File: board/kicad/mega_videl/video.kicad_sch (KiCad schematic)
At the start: 18 parts, among them U15 PCA9546APWR, U19 TMDS1204IRNQR, U20 TPD4E02B04DQA, U21 TPD4E02B04DQA, U22 TPD4E02B04DQA, U8 XLH335074.250000X

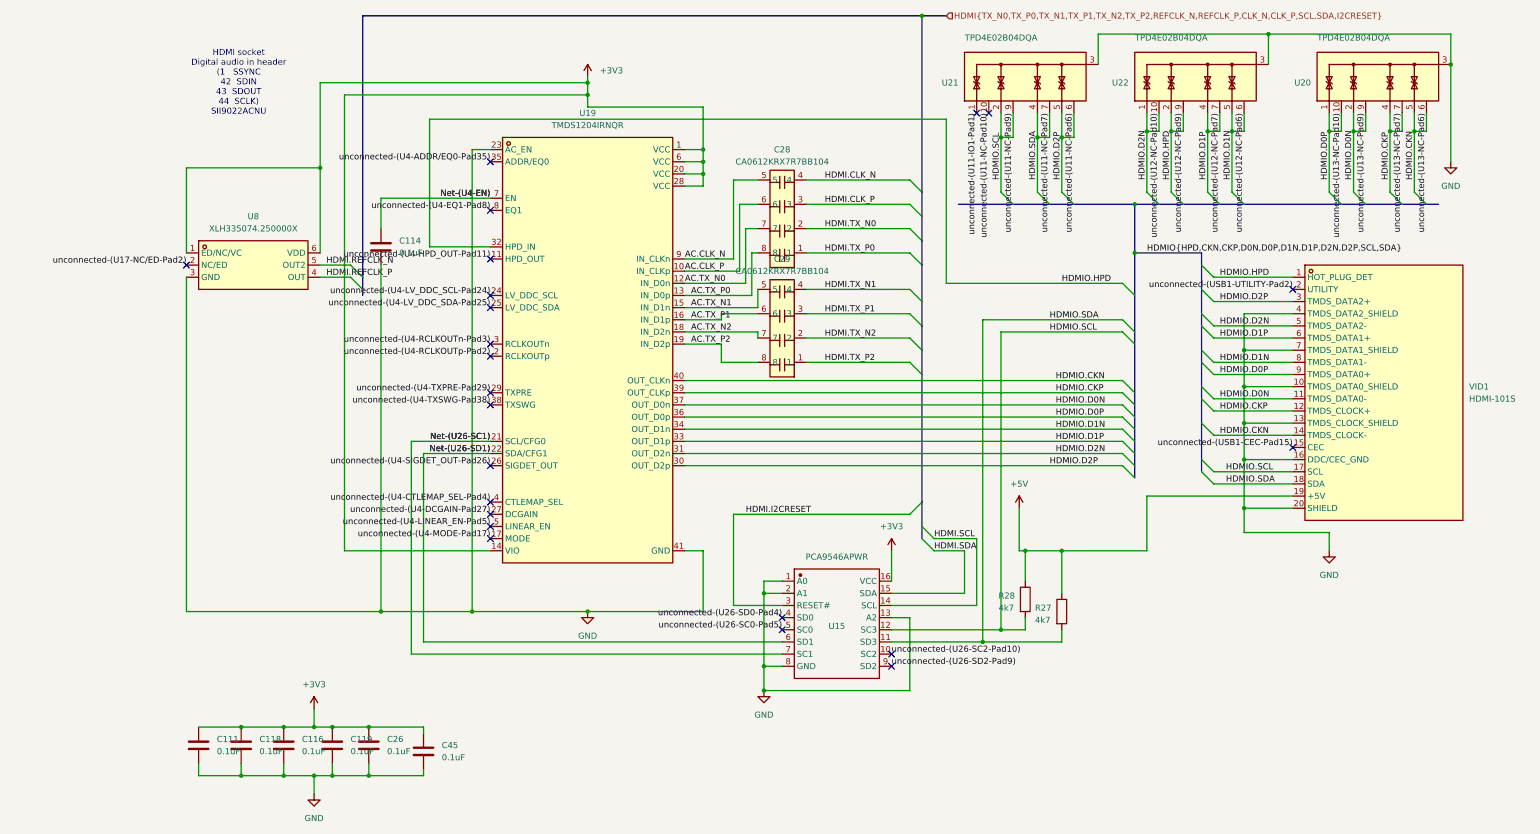
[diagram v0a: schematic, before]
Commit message: Reviewed and fixed many issues. e.g. missing decoupling for 1.35v under fpga
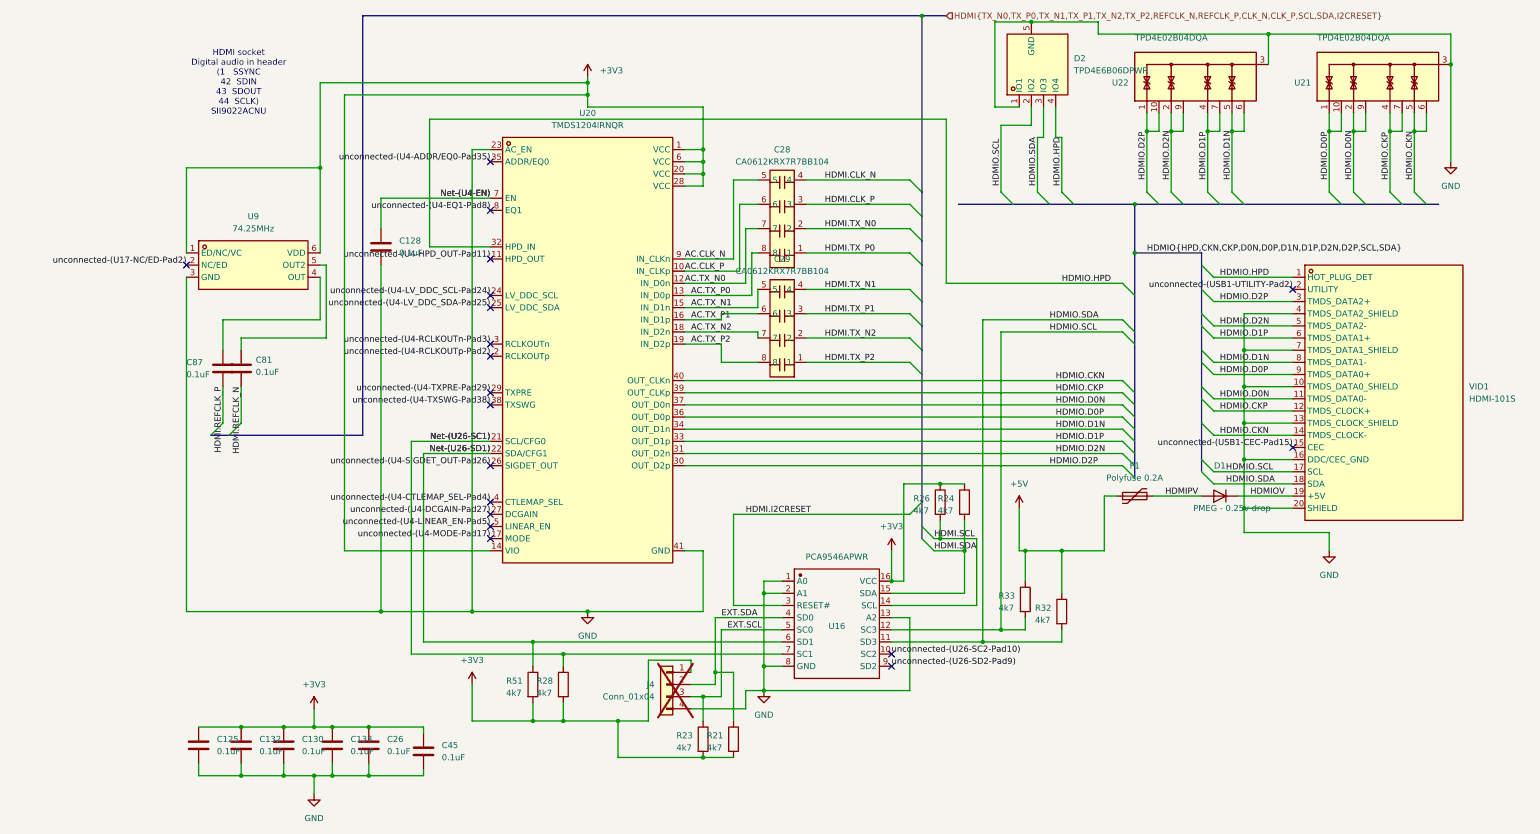
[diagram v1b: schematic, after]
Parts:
- removed U21: TPD4E02B04DQA, Package_SON:USON-10_2.5x1.0mm_P0.5mm, symbol Power_Protection:TPD4E02B04DQA
- added C81, C87: 0.1uF, Capacitor_SMD:C_0402_1005Metric, symbol Device:C
- added D1: PMEG - 0.25v drop, Diode_SMD:D_0603_1608Metric, symbol Device:D
- added D2: TPD4E6B06DPWR, mega_videl:X2SON-4_L0.8-W0.8-P0.48-TL-A, symbol mega_videl:TPD4E6B06DPWR
- added F1: Polyfuse 0.2A, Resistor_SMD:R_0603_1608Metric, symbol Device:Polyfuse
- added J4: Conn_01x04, Connector_PinHeader_2.54mm:PinHeader_1x04_P2.54mm_Vertical, symbol Connector_Generic:Conn_01x04
- added R21, R23, R24, R26, R28, R51: 4k7, Resistor_SMD:R_0603_1608Metric, symbol Device:R
- U16: renamed from U15; LCSC Part (none) -> C400705
- U9: renamed from U8; value XLH335074.250000X -> 74.25MHz; LCSC Part C1883920 -> C836732; MPN XLH335074.250000X -> SiT9121AC-2B2-33E74.250000; Manufacturer RENESAS(瑞萨)/IDT -> SiTime
- renumbered C111 to C125, C114 to C128, C116 to C130, C118 to C132, C119 to C133, R27 to R32, R28 to R33, U19 to U20, U20 to U21
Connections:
- net +3V3: now also J4.1 (Pin_1), R21.2, R23.2, R24.1, R26.1, R28.2, R51.2
- net +5V: now also F1.1; no longer VID1.19 (+5V)
- net GND: now also D2.1 (IO1), D2.5 (GND), J4.4 (Pin_4)
- net HDMI.REFCLK_N: now also C81.1; no longer U9.5 (OUT2)
- net HDMI.REFCLK_P: now also C87.1; no longer U9.4 (OUT)
- net HDMI.SCL: now also R26.2
- net HDMI.SDA: now also R24.2
- net HDMIO.D2N: now also U22.2 (IO2), U22.9 (NC); no longer U22.1 (IO1), U22.10 (NC)
- net HDMIO.D2P: now also U22.1 (IO1), U22.10 (NC)
- net HDMIO.HPD: now also D2.4 (IO4); no longer U22.2 (IO2), U22.9 (NC)
- net HDMIO.SCL: now also D2.2 (IO2)
- net HDMIO.SDA: now also D2.3 (IO3)
- net Net-(U26-SC1): now also R28.1
- net Net-(U26-SD1): now also R51.1
- net unconnected-(U26-SC0-Pad5) renamed EXT.SCL
- net EXT.SCL: now also J4.3 (Pin_3), R23.1
- net unconnected-(U26-SD0-Pad4) renamed EXT.SDA
- net EXT.SDA: now also J4.2 (Pin_2), R21.1
- new net: C81.2, U9.5 (OUT2)
- new net: C87.2, U9.4 (OUT)
- new net HDMIOV: D1.1 (K), VID1.19 (+5V)
- new net HDMIPV: D1.2 (A), F1.2
- no-connect marks 23 -> 19

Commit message: Assigned all parts with JLCPCB plugin
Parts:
- C125, C128, C130, C132, C133, C26, C45: LCSC (none) -> C14663
- C81, C87: LCSC (none) -> C1525
- D1: footprint Diode_SMD:D_0603_1608Metric -> Diode_SMD:D_SOD-323; LCSC (none) -> C7420331
- F1: LCSC (none) -> C207011
- R21, R23, R24, R26, R28, R32, R33, R51: LCSC (none) -> C23162
- U21, U22: LCSC (none) -> C106794
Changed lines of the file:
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@@
 			)
 		)
-		(property "Footprint" "Diode_SMD:D_0603_1608Metric"
+		(property "Footprint" "Diode_SMD:D_SOD-323"
 			(at 232.41 128.27 0)
 			(hide yes)
@@
 			)
 		)
+		(property "LCSC" "C7420331"
+			(at 232.41 128.27 0)
+			(hide yes)
+			(show_name no)
+			(do_not_autoplace no)
+			(effects
+				(font
+					(size 1.27 1.27)
+				)
+			)
+		)
 		(pin "1"
 		)
@@
 			)
 		)
+		(property "LCSC" "C14663"
+			(at 66.04 181.61 0)
+			(hide yes)
+			(show_name no)
+			(do_not_autoplace no)
+			(effects
+				(font
+					(size 1.27 1.27)
+				)
+			)
+		)
 		(pin "1"
 		)
@@
 			)
 		)
+		(property "LCSC" "C23162"
+			(at 179.07 129.54 0)
+			(hide yes)
+			(show_name no)
+			(do_not_autoplace no)
+			(effects
+				(font
+					(size 1.27 1.27)
+				)
+			)
+		)
 		(pin "1"
 		)
@@
 			)
 		)
+		(property "LCSC" "C1525"
+			(at 27.94 101.6 0)
+			(hide yes)
+			(show_name no)
+			(do_not_autoplace no)
+			(effects
+				(font
+					(size 1.27 1.27)
+				)
+			)
+		)
 		(pin "1"
 		)
@@
 			)
 		)
+		(property "LCSC" "C14663"
+			(at 54.61 180.34 0)
+			(hide yes)
+			(show_name no)
+			(do_not_autoplace no)
+			(effects
+				(font
+					(size 1.27 1.27)
+				)
+			)
+		)
 		(pin "1"
 		)
@@
 			)
 		)
+		(property "LCSC" "C23162"
+			(at 199.39 152.4 0)
+			(hide yes)
+			(show_name no)
+			(do_not_autoplace no)
+			(effects
+				(font
+					(size 1.27 1.27)
+				)
+			)
+		)
 		(pin "1"
 		)
@@
 			)
 		)
+		(property "LCSC" "C23162"
+			(at 130.81 179.07 0)
+			(hide yes)
+			(show_name no)
+			(do_not_autoplace no)
+			(effects
+				(font
+					(size 1.27 1.27)
+				)
+			)
+		)
 		(pin "1"
 		)
@@
 			)
 		)
+		(property "LCSC" "C1525"
+			(at 24.13 101.6 0)
+			(hide yes)
+			(show_name no)
+			(do_not_autoplace no)
+			(effects
+				(font
+					(size 1.27 1.27)
+				)
+			)
+		)
 		(pin "1"
 		)
@@
 			)
 		)
+		(property "LCSC" "C23162"
+			(at 88.9 167.64 0)
+			(hide yes)
+			(show_name no)
+			(do_not_autoplace no)
+			(effects
+				(font
+					(size 1.27 1.27)
+				)
+			)
+		)
 		(pin "1"
 		)
@@
 			)
 		)
+		(property "LCSC" "C14663"
+			(at 46.99 180.34 0)
+			(hide yes)
+			(show_name no)
+			(do_not_autoplace no)
+			(effects
+				(font
+					(size 1.27 1.27)
+				)
+			)
+		)
 		(pin "1"
 		)
@@
 			)
 		)
+		(property "LCSC" "C23162"
+			(at 124.46 179.07 0)
+			(hide yes)
+			(show_name no)
+			(do_not_autoplace no)
+			(effects
+				(font
+					(size 1.27 1.27)
+				)
+			)
+		)
 		(pin "1"
 		)
@@
 			)
 		)
+		(property "LCSC" "C23162"
+			(at 173.99 129.54 0)
+			(hide yes)
+			(show_name no)
+			(do_not_autoplace no)
+			(effects
+				(font
+					(size 1.27 1.27)
+				)
+			)
+		)
 		(pin "1"
 		)
@@
 			)
 		)
+		(property "LCSC" "C106794"
+			(at 265.43 40.64 0)
+			(hide yes)
+			(show_name no)
+			(do_not_autoplace no)
+			(effects
+				(font
+					(size 1.27 1.27)
+				)
+			)
+		)
 		(pin "4"
 		)
@@
 			)
 		)
+		(property "LCSC" "C207011"
+			(at 214.63 128.27 0)
+			(hide yes)
+			(show_name no)
+			(do_not_autoplace no)
+			(effects
+				(font
+					(size 1.27 1.27)
+				)
+			)
+		)
 		(pin "1"
 		)
@@
 			)
 		)
+		(property "LCSC" "C14663"
+			(at 36.83 180.34 0)
+			(hide yes)
+			(show_name no)
+			(do_not_autoplace no)
+			(effects
+				(font
+					(size 1.27 1.27)
+				)
+			)
+		)
 		(pin "1"
 		)
@@
 			)
 		)
+		(property "LCSC" "C14663"
+			(at 27.94 180.34 0)
+			(hide yes)
+			(show_name no)
+			(do_not_autoplace no)
+			(effects
+				(font
+					(size 1.27 1.27)
+				)
+			)
+		)
 		(pin "1"
 		)
@@
 			)
 		)
+		(property "LCSC" "C106794"
+			(at 227.33 40.64 0)
+			(hide yes)
+			(show_name no)
+			(do_not_autoplace no)
+			(effects
+				(font
+					(size 1.27 1.27)
+				)
+			)
+		)
 		(pin "4"
 		)
@@
 			)
 		)
+		(property "LCSC" "C23162"
+			(at 191.77 149.86 0)
+			(hide yes)
+			(show_name no)
+			(do_not_autoplace no)
+			(effects
+				(font
+					(size 1.27 1.27)
+				)
+			)
+		)
 		(pin "1"
 		)
@@
 			)
 		)
+		(property "LCSC" "C14663"
+			(at 19.05 180.34 0)
+			(hide yes)
+			(show_name no)
+			(do_not_autoplace no)
+			(effects
+				(font
+					(size 1.27 1.27)
+				)
+			)
+		)
 		(pin "1"
 		)
@@
 			)
 		)
+		(property "LCSC" "C23162"
+			(at 95.25 167.64 0)
+			(hide yes)
+			(show_name no)
+			(do_not_autoplace no)
+			(effects
+				(font
+					(size 1.27 1.27)
+				)
+			)
+		)
 		(pin "1"
 		)
@@
 			(at 57.15 76.2 0)
 			(hide yes)
+			(show_name no)
+			(do_not_autoplace no)
+			(effects
+				(font
+					(size 1.27 1.27)
+				)
+			)
+		)
+		(property "LCSC" "C14663"
+			(at 57.15 76.2 0)
+			(hide yes)

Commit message: Added series resistors to all CT lines. They ring up to 7V apparently according to Super Videl devs. Some of that is likely the length of scope lines. The safety fix here is to add small 33ohm resistors and to enable clamp diodes in the FPGA core.
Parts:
- U20: LCSC Part C20345954 -> C19272424
- renumbered R51 to R137, R21 to R37, R23 to R40, R24 to R43, R26 to R45, R28 to R47, R32 to R51, R33 to R52
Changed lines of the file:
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@@
 			)
 		)
-		(property "LCSC Part" "C20345954"
+		(property "LCSC Part" "C19272424"
 			(at 100.33 157.48 0)
 			(hide yes)
@@
 		(in_pos_files yes)
 		(dnp no)
-		(property "Reference" "R24"
+		(property "Reference" "R43"
 			(at 173.482 128.778 0)
 			(show_name no)
@@
 			(project "mega_videl"
 				(path "/10511203-7d65-4cdf-a1a4-c07b44ea87e2/198460ff-814d-446f-8f27-49d102cbfcc8"
-					(reference "R24")
+					(reference "R43")
 					(unit 1)
 				)
@@
 		(in_pos_files yes)
 		(dnp no)
-		(property "Reference" "R32"
+		(property "Reference" "R51"
 			(at 193.802 151.638 0)
 			(show_name no)
@@
 			(project "mega_videl"
 				(path "/10511203-7d65-4cdf-a1a4-c07b44ea87e2/198460ff-814d-446f-8f27-49d102cbfcc8"
-					(reference "R32")
+					(reference "R51")
 					(unit 1)
 				)
@@
 		(in_pos_files yes)
 		(dnp no)
-		(property "Reference" "R21"
+		(property "Reference" "R37"
 			(at 125.222 178.308 0)
 			(show_name no)
@@
 			(project "mega_videl"
 				(path "/10511203-7d65-4cdf-a1a4-c07b44ea87e2/198460ff-814d-446f-8f27-49d102cbfcc8"
-					(reference "R21")
+					(reference "R37")
 					(unit 1)
 				)
@@
 		(in_pos_files yes)
 		(dnp no)
-		(property "Reference" "R51"
+		(property "Reference" "R137"
 			(at 83.312 166.878 0)
 			(show_name no)
@@
 			(project "mega_videl"
 				(path "/10511203-7d65-4cdf-a1a4-c07b44ea87e2/198460ff-814d-446f-8f27-49d102cbfcc8"
-					(reference "R51")
+					(reference "R137")
 					(unit 1)
 				)
@@
 		(in_pos_files yes)
 		(dnp no)
-		(property "Reference" "R23"
+		(property "Reference" "R40"
 			(at 118.872 178.308 0)
 			(show_name no)
@@
 			(project "mega_videl"
 				(path "/10511203-7d65-4cdf-a1a4-c07b44ea87e2/198460ff-814d-446f-8f27-49d102cbfcc8"
-					(reference "R23")
+					(reference "R40")
 					(unit 1)
 				)
@@
 		(in_pos_files yes)
 		(dnp no)
-		(property "Reference" "R26"
+		(property "Reference" "R45"
 			(at 168.402 128.778 0)
 			(show_name no)
@@
 			(project "mega_videl"
 				(path "/10511203-7d65-4cdf-a1a4-c07b44ea87e2/198460ff-814d-446f-8f27-49d102cbfcc8"
-					(reference "R26")
+					(reference "R45")
 					(unit 1)
 				)
@@
 		(in_pos_files yes)
 		(dnp no)
-		(property "Reference" "R33"
+		(property "Reference" "R52"
 			(at 186.182 149.098 0)
 			(show_name no)
@@
 			(project "mega_videl"
 				(path "/10511203-7d65-4cdf-a1a4-c07b44ea87e2/198460ff-814d-446f-8f27-49d102cbfcc8"
-					(reference "R33")
+					(reference "R52")
 					(unit 1)
 				)
@@
 		(in_pos_files yes)
 		(dnp no)
-		(property "Reference" "R28"
+		(property "Reference" "R47"
 			(at 89.662 166.878 0)
 			(show_name no)
@@
 			(project "mega_videl"
 				(path "/10511203-7d65-4cdf-a1a4-c07b44ea87e2/198460ff-814d-446f-8f27-49d102cbfcc8"
-					(reference "R28")
+					(reference "R47")
 					(unit 1)
 				)

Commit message: Shrunk the dimensions to fit better so it does not hit Q1. Added a notch for the DIMM casing.
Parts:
- C128, C130, C133: footprint Capacitor_SMD:C_0603_1608Metric -> Capacitor_SMD:C_0402_1005Metric
- J4: now left out of the parts list
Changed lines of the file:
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@@
 			)
 		)
-		(property "Footprint" "Capacitor_SMD:C_0603_1608Metric"
+		(property "Footprint" "Capacitor_SMD:C_0402_1005Metric"
 			(at 47.9552 184.15 0)
 			(hide yes)
@@
 		(body_style 1)
 		(exclude_from_sim no)
-		(in_bom yes)
-		(on_board yes)
-		(in_pos_files yes)
+		(in_bom no)
+		(on_board yes)
+		(in_pos_files no)
 		(dnp yes)
 		(property "Reference" "J4"
@@
 			)
 		)
-		(property "Footprint" "Capacitor_SMD:C_0603_1608Metric"
+		(property "Footprint" "Capacitor_SMD:C_0402_1005Metric"
 			(at 37.7952 184.15 0)
 			(hide yes)
@@
 			)
 		)
-		(property "Footprint" "Capacitor_SMD:C_0603_1608Metric"
+		(property "Footprint" "Capacitor_SMD:C_0402_1005Metric"
 			(at 58.1152 80.01 0)
 			(hide yes)

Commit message: Fix some 0603s that had an 0402 part by mistake
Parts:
- C128, C130, C133: KiLib_Generator (none) -> SMD_2terminal_chip_molded; LCSC C14663 -> C1525
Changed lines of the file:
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@@
 			)
 		)
-		(property "LCSC" "C14663"
+		(property "LCSC" "C1525"
+			(at 46.99 180.34 0)
+			(hide yes)
+			(show_name no)
+			(do_not_autoplace no)
+			(effects
+				(font
+					(size 1.27 1.27)
+				)
+			)
+		)
+		(property "KiLib_Generator" "SMD_2terminal_chip_molded"
 			(at 46.99 180.34 0)
 			(hide yes)
@@
 			)
 		)
-		(property "LCSC" "C14663"
+		(property "LCSC" "C1525"
+			(at 36.83 180.34 0)
+			(hide yes)
+			(show_name no)
+			(do_not_autoplace no)
+			(effects
+				(font
+					(size 1.27 1.27)
+				)
+			)
+		)
+		(property "KiLib_Generator" "SMD_2terminal_chip_molded"
 			(at 36.83 180.34 0)
 			(hide yes)
@@
 			)
 		)
-		(property "LCSC" "C14663"
+		(property "LCSC" "C1525"
 			(at 57.15 76.2 0)
 			(hide yes)
+			(show_name no)
+			(do_not_autoplace no)
+			(effects
+				(font
+					(size 1.27 1.27)
+				)
+			)
+		)
+		(property "KiLib_Generator" "SMD_2terminal_chip_molded"
+			(at 57.15 76.2 0)
+			(hide yes)
